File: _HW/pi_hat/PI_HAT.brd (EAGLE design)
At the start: 65 x 57.5 mm, 19 parts, among them J2 RASPBERRYPI-40-PIN-GPIO_SMD_S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

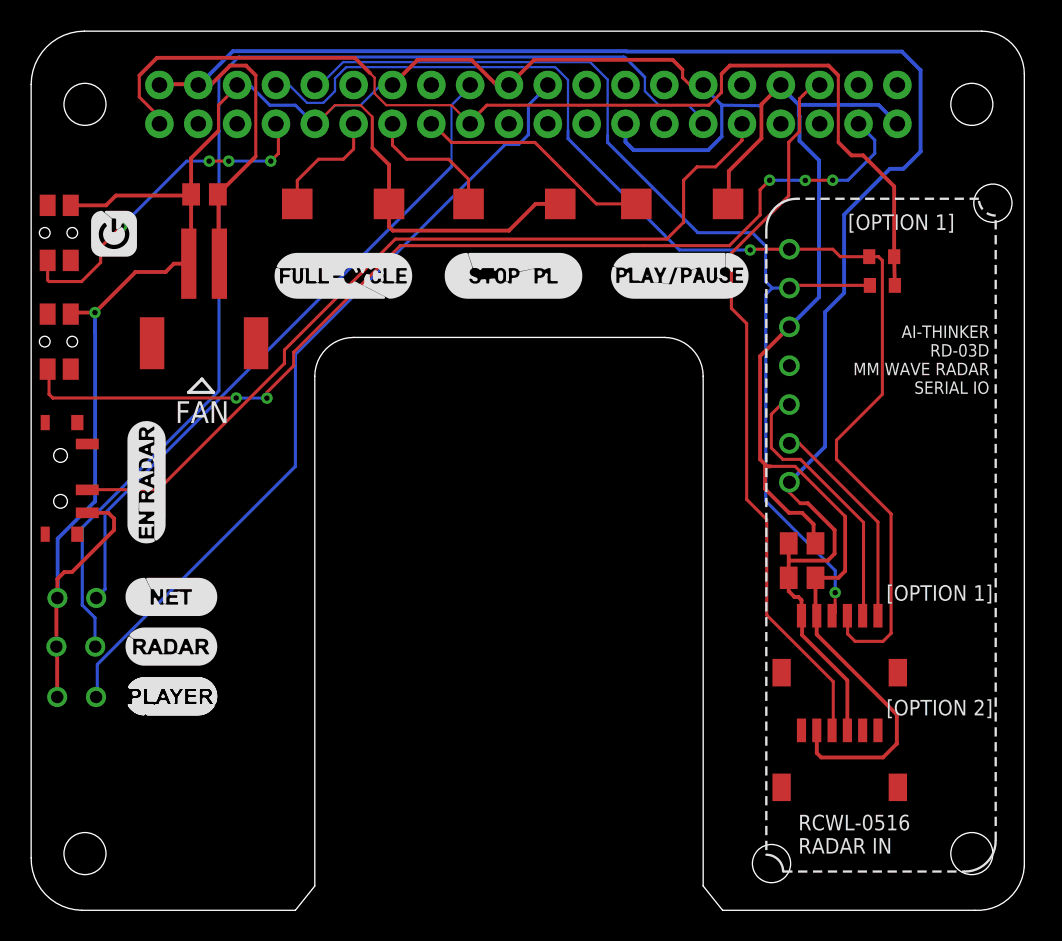
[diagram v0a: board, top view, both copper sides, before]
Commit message: Added PCB V2 data
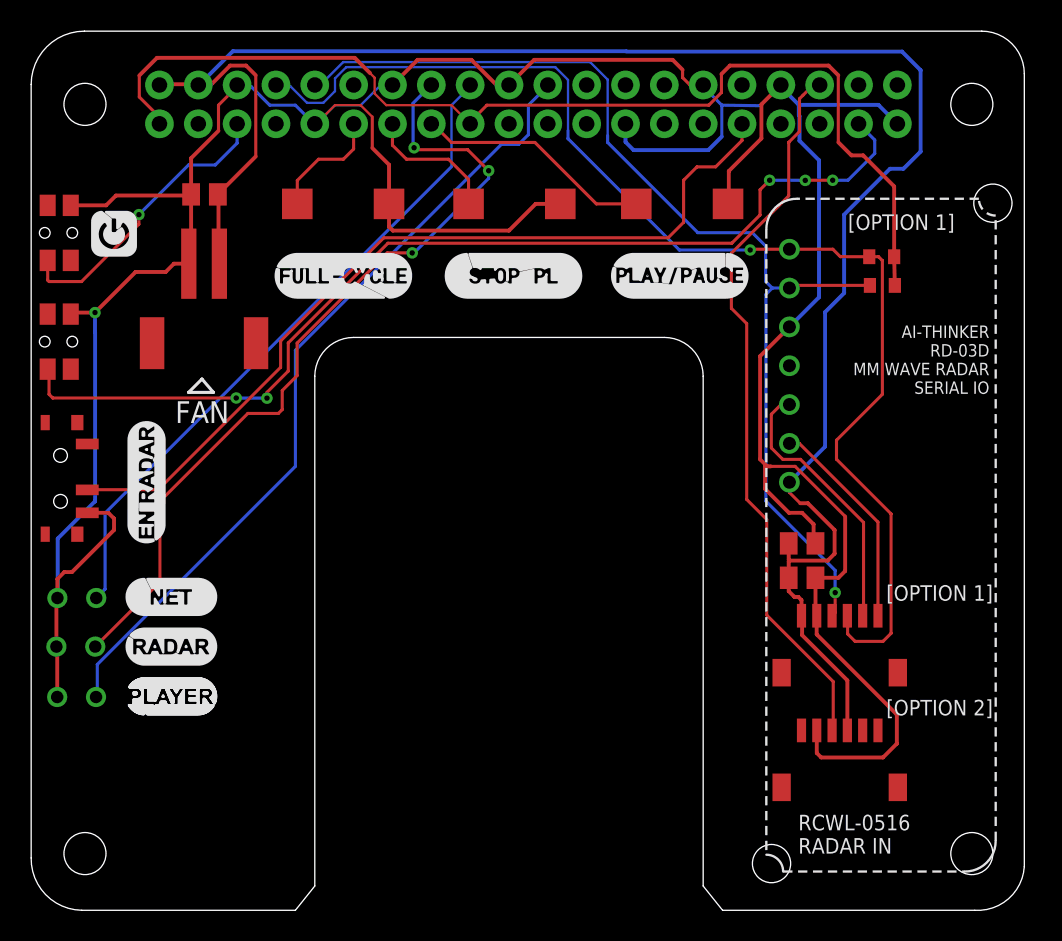
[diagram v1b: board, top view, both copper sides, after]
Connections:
- removed net BTN_NET_RESET: J2.16
- net BTN_POWER: now also J2.5; no longer J2.7
- net LED_RADAR_STATE: now also J2.16; no longer J2.29
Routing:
- net LED_RADAR_STATE: track 76.0 -> 54.1 mm, vias 0 -> 3
- net BTN_POWER: track 22.5 -> 19.1 mm, vias 4 -> 1
- net NET_RESET_BTN: track 66.5 -> 67.1 mm
